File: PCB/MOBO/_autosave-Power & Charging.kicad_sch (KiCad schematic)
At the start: 46 parts, among them J201 USB_C_Receptacle_PowerOnly_6P, Q1 PMOS, Q2 NMOS, Q3 NMOS, Q4 NMOS, SW1 SW_DPST_x2, U1 BQ297xy, U2 AT90USB647-M, U202 MCP73871-1AA, U205 TPS61230DRC

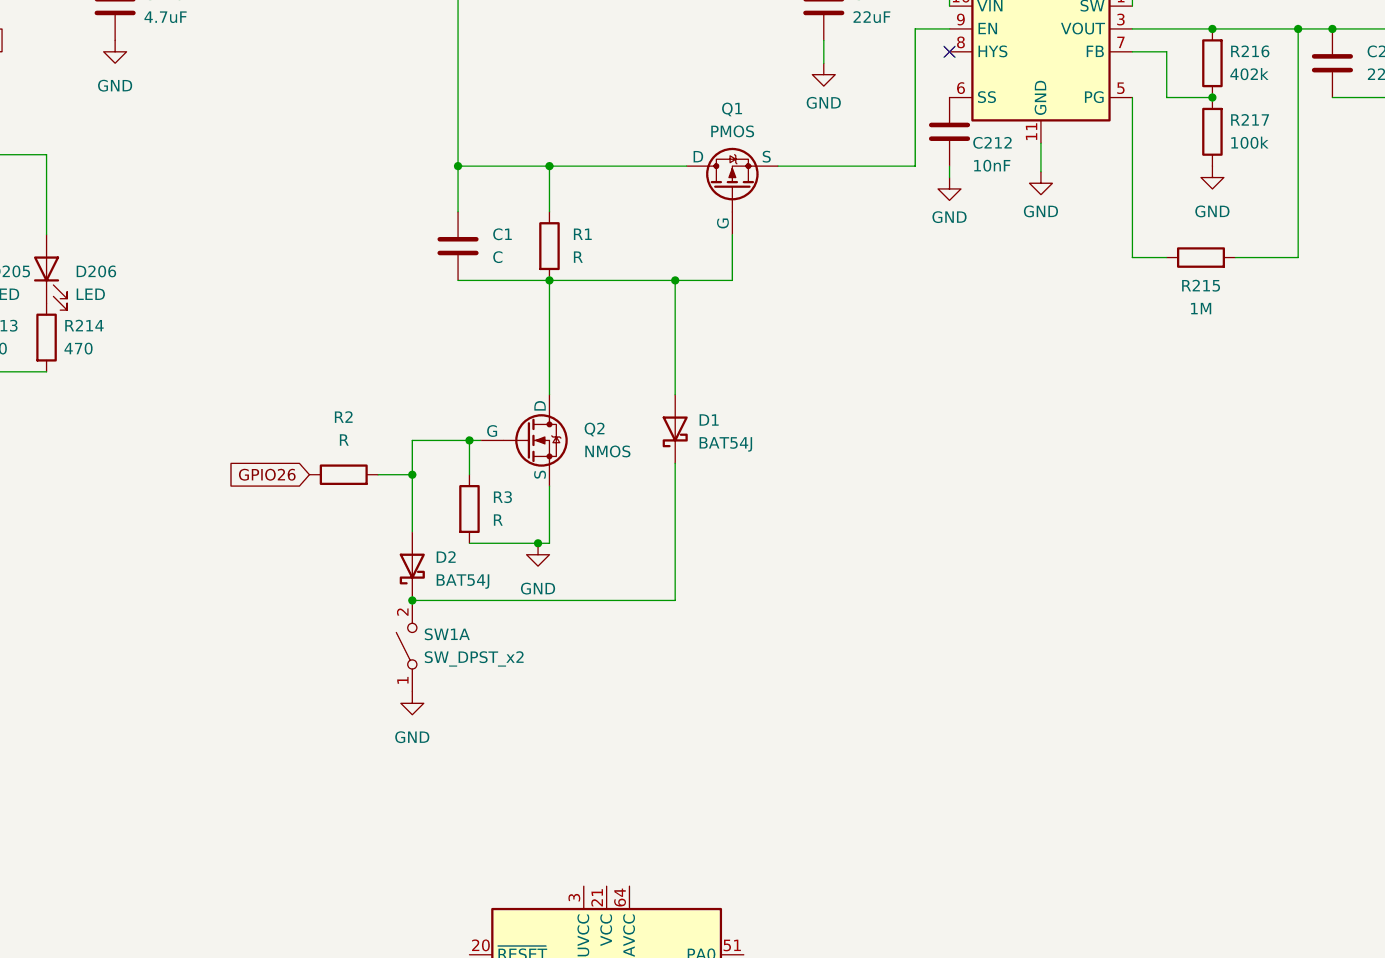
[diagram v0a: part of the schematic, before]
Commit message: added safe latch controlled shutdown
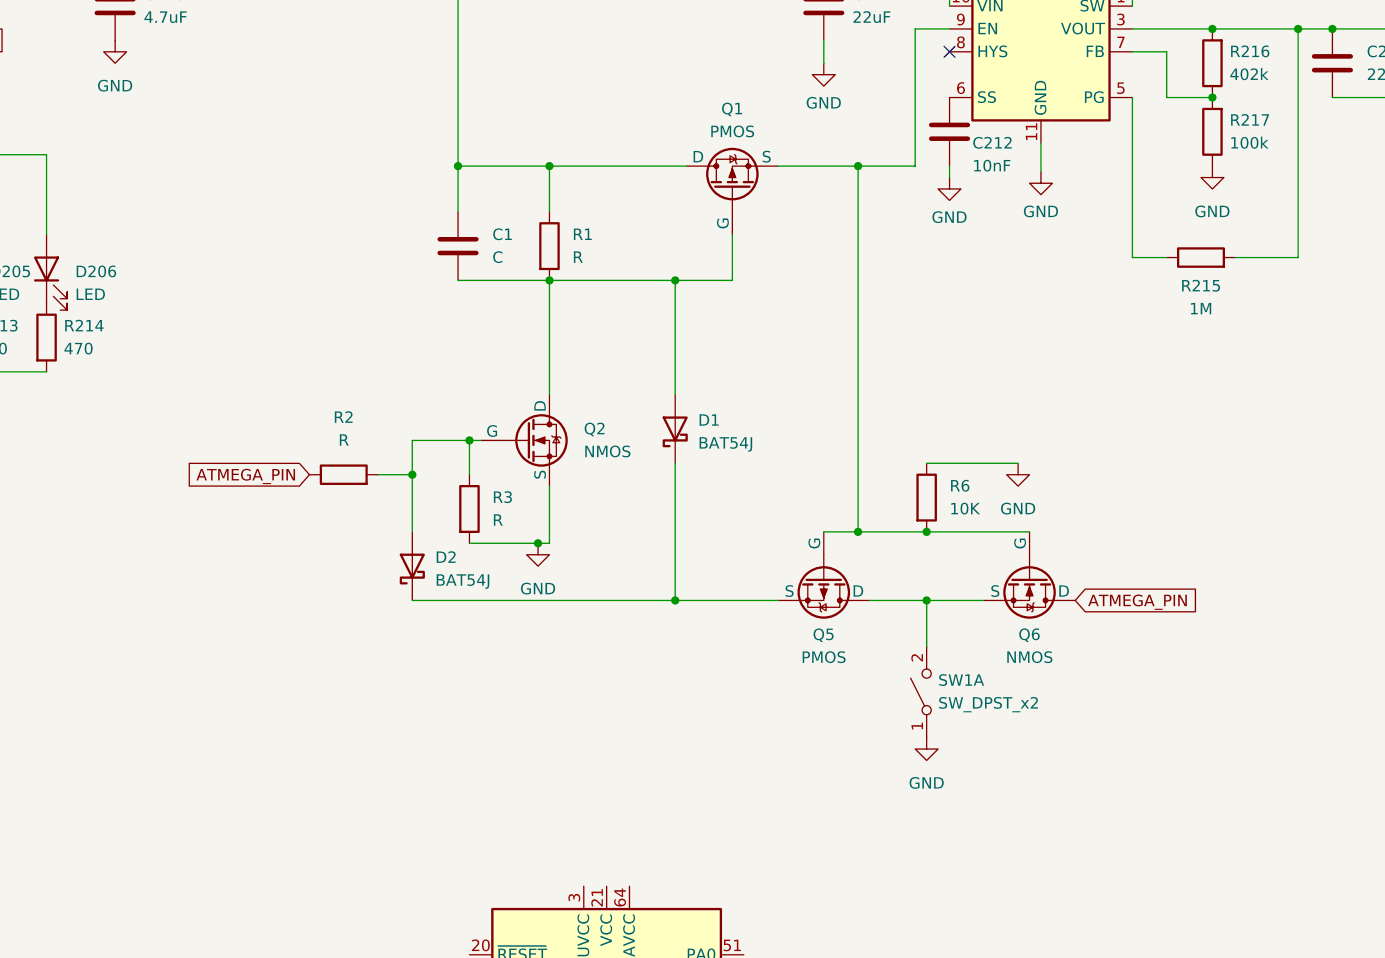
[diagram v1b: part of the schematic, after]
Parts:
- added Q5: PMOS, symbol Simulation_SPICE:PMOS
- added Q6: NMOS, symbol Simulation_SPICE:NMOS
- added R6: 10K, symbol Device:R
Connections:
- net GND: now also R6.1
- net at D1.1 (K), D2.1 (K): now also Q5.3 (S); no longer SW1.2 (B)
- net at Q1.3 (S), U205.9 (EN): now also Q5.2 (G), Q6.2 (G), R6.2
- net GPIO26 renamed ATMEGA_PIN
- net ATMEGA_PIN: now also Q6.1 (D)
- new net: Q5.1 (D), Q6.3 (S), SW1.2 (B)
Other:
- moved on the sheet: SW1A
